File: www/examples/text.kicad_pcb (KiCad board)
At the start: 2 copper layers, 223.5 x 71.1 mm, 0 parts

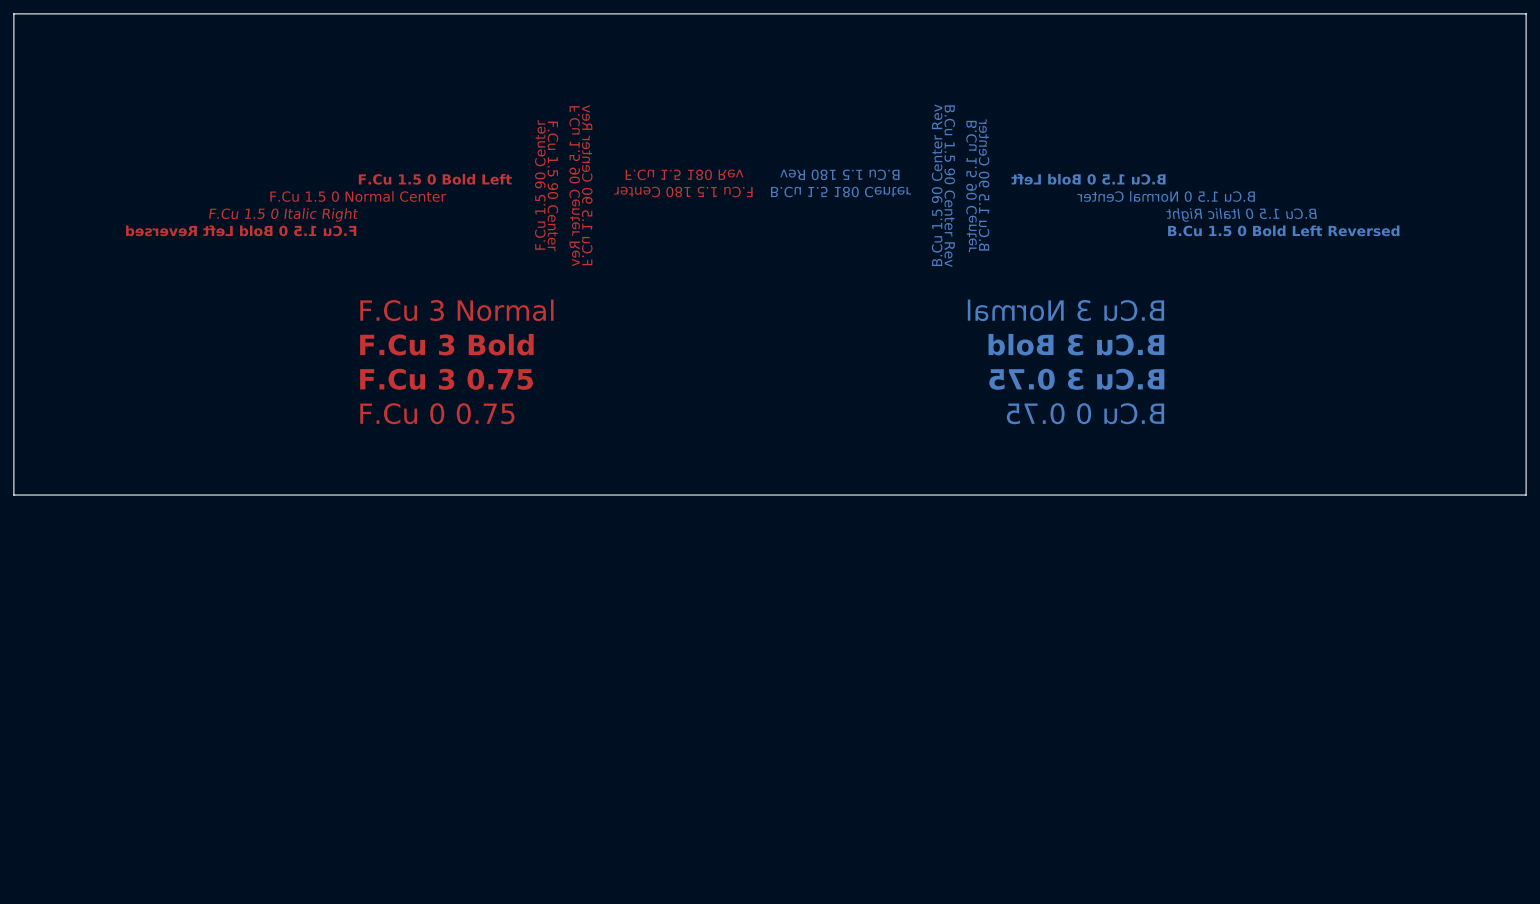
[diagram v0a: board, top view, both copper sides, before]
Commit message: Use new text engine for FpText
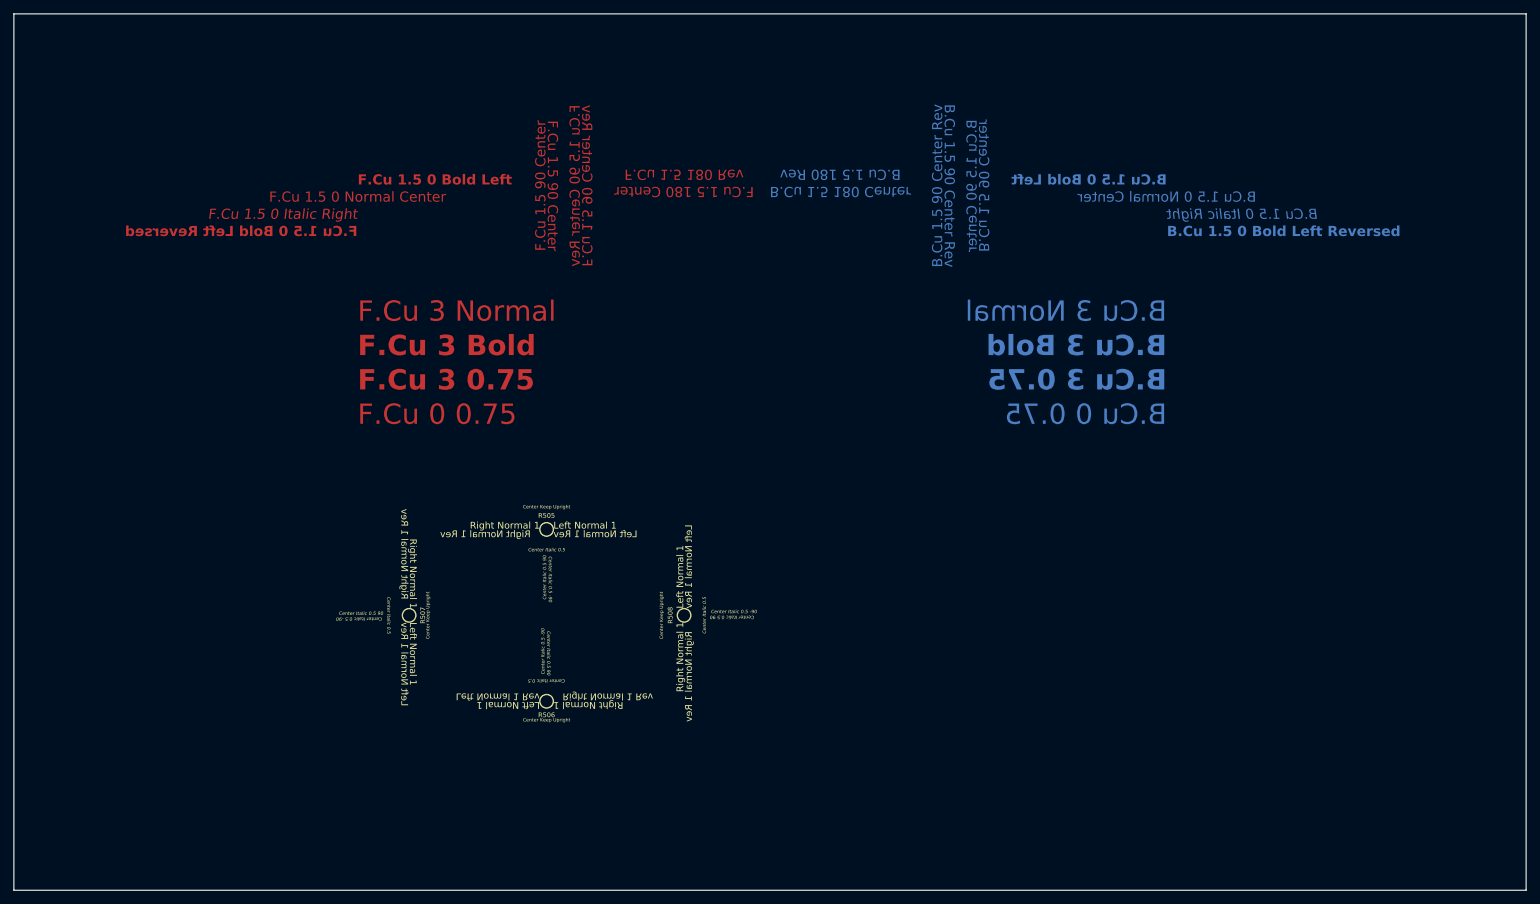
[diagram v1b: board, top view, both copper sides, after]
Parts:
- added R505: 10k, winterbloom:R_0402_HandSolder, F.Cu at (27.9, 50.8)
- added R505: 10k, winterbloom:R_0402_HandSolder, B.Cu at (94.0, 50.8)
- added R505: 10k, winterbloom:R_0402_HandSolder, B.Cu at (73.7, 63.5)
- added R505: 10k, winterbloom:R_0402_HandSolder, B.Cu at (94.0, 76.2)
- added R505: 10k, winterbloom:R_0402_HandSolder, B.Cu at (114.3, 63.5)
- added R506: 10k, winterbloom:R_0402_HandSolder, F.Cu at (27.9, 76.2)
- added R507: 10k, winterbloom:R_0402_HandSolder, F.Cu at (7.62, 63.5)
- added R508: 10k, winterbloom:R_0402_HandSolder, F.Cu at (48.3, 63.5)
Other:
- board size 223.5 x 71.1 mm -> 223.5 x 129.5 mm

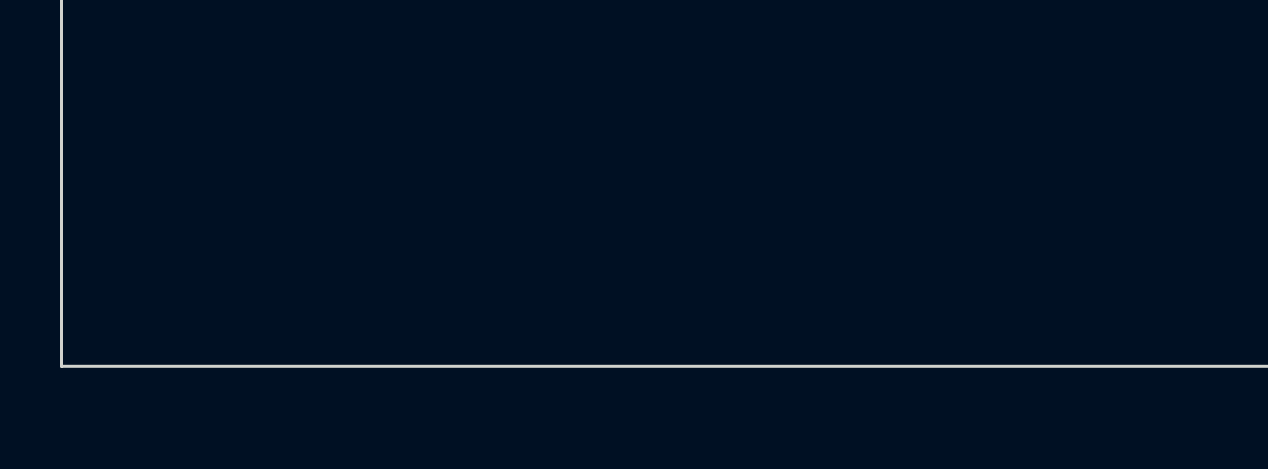
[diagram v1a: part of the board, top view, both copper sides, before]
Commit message: Add examples of custom fonts in text examples
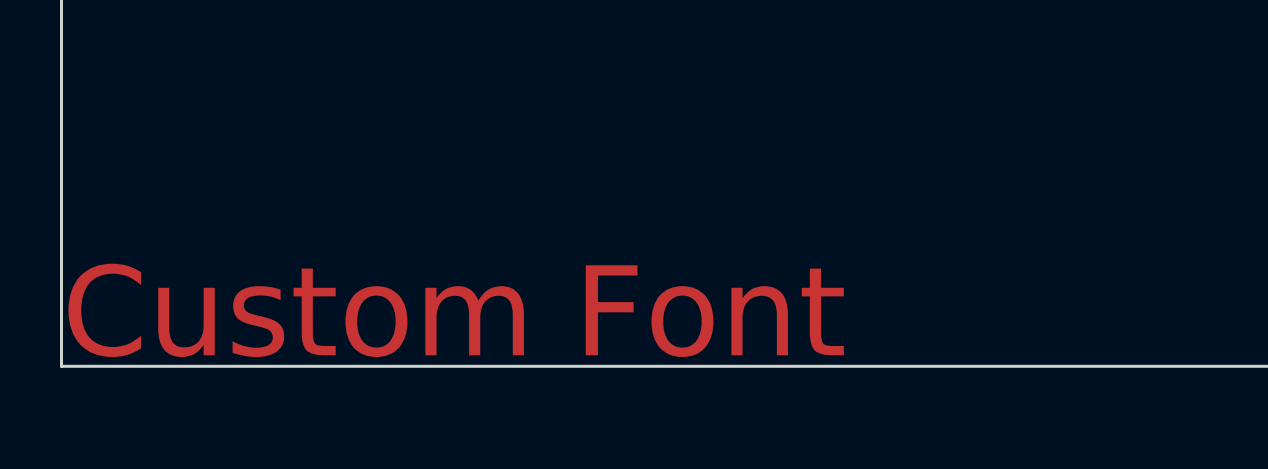
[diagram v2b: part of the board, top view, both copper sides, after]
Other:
- board text added: "Custom Font"

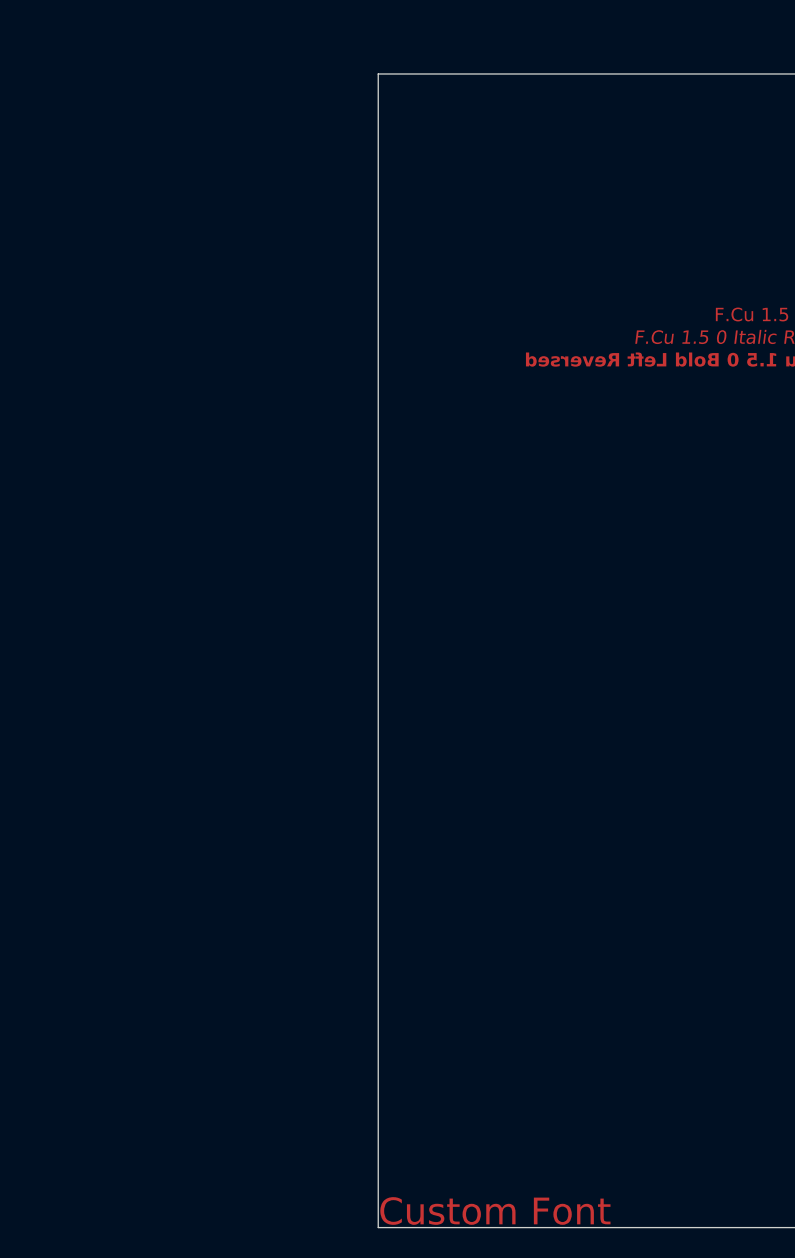
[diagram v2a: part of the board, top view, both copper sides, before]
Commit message: Fix bug in angle.rotate_point
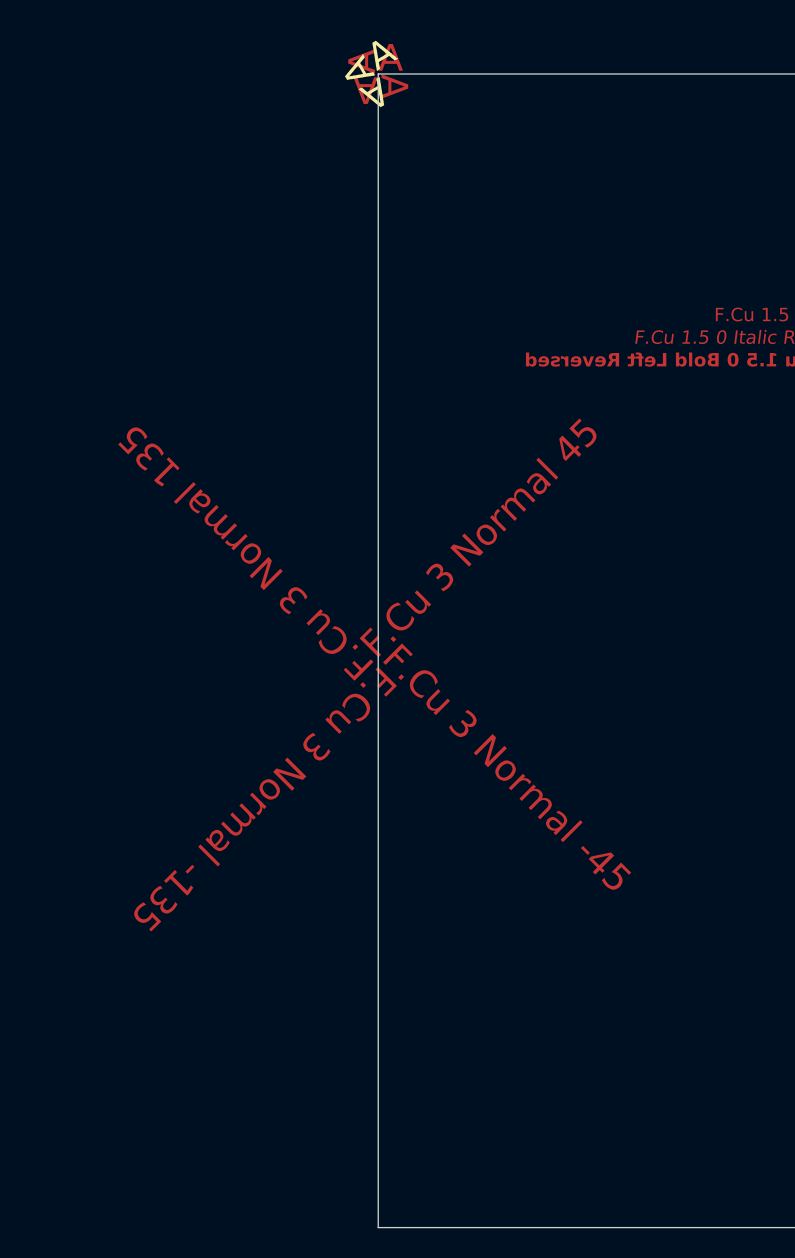
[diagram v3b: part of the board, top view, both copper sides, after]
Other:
- board text added: "A"
- board text added: "F.Cu 3 Normal -135"
- board text added: "F.Cu 3 Normal -45"
- board text added: "F.Cu 3 Normal 135"
- board text added: "F.Cu 3 Normal 45"
- board text removed: "Custom Font"

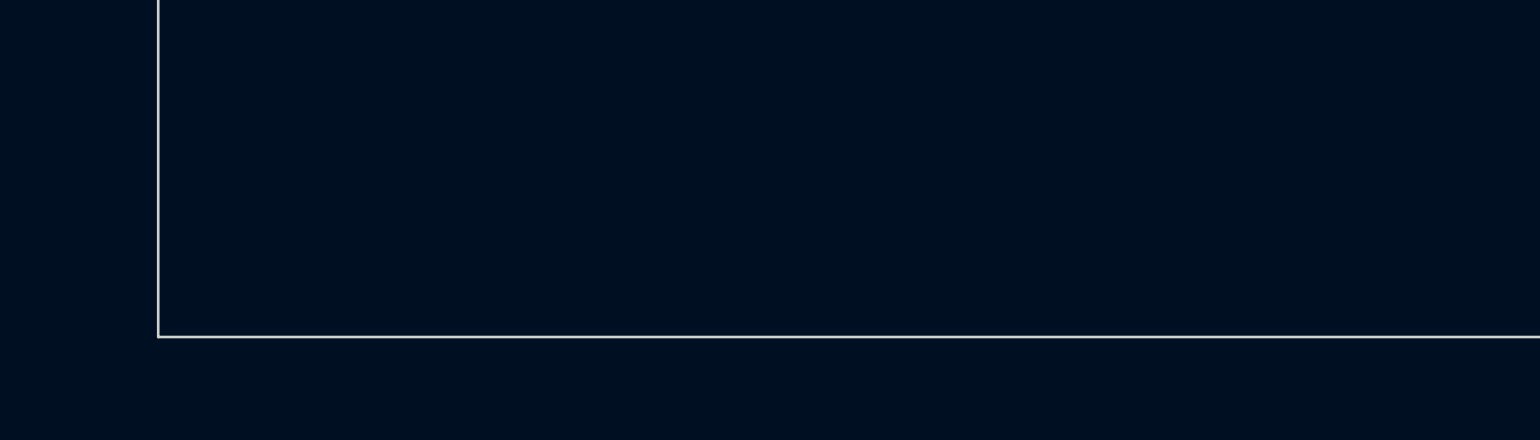
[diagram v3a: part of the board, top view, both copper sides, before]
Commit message: Add support for KiCAD 7's render_cache for board items with custom fonts.
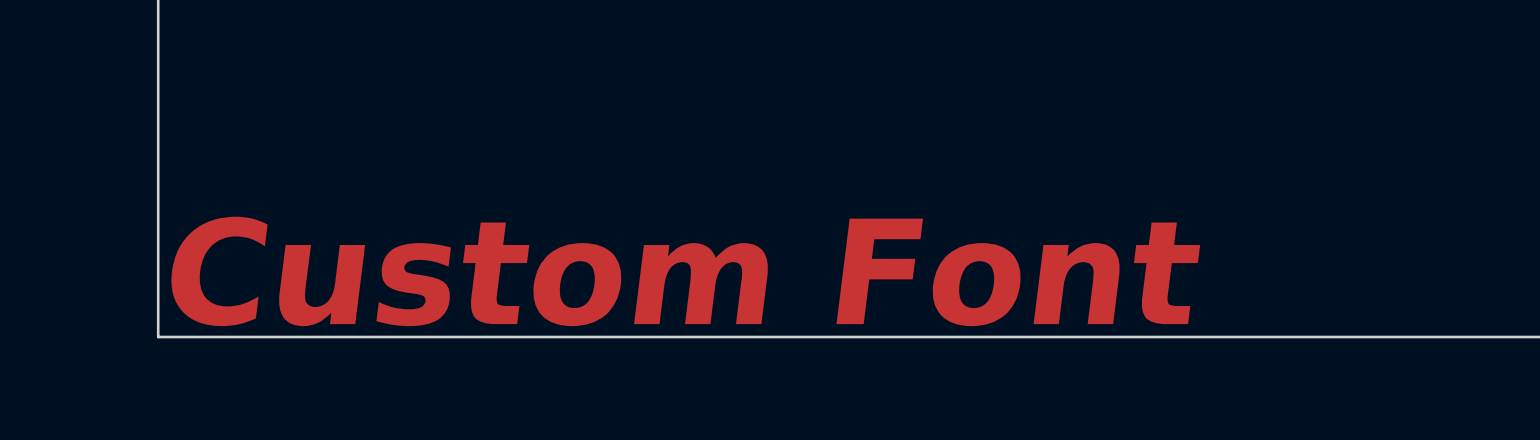
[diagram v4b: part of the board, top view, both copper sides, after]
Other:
- board text added: "Custom Font"

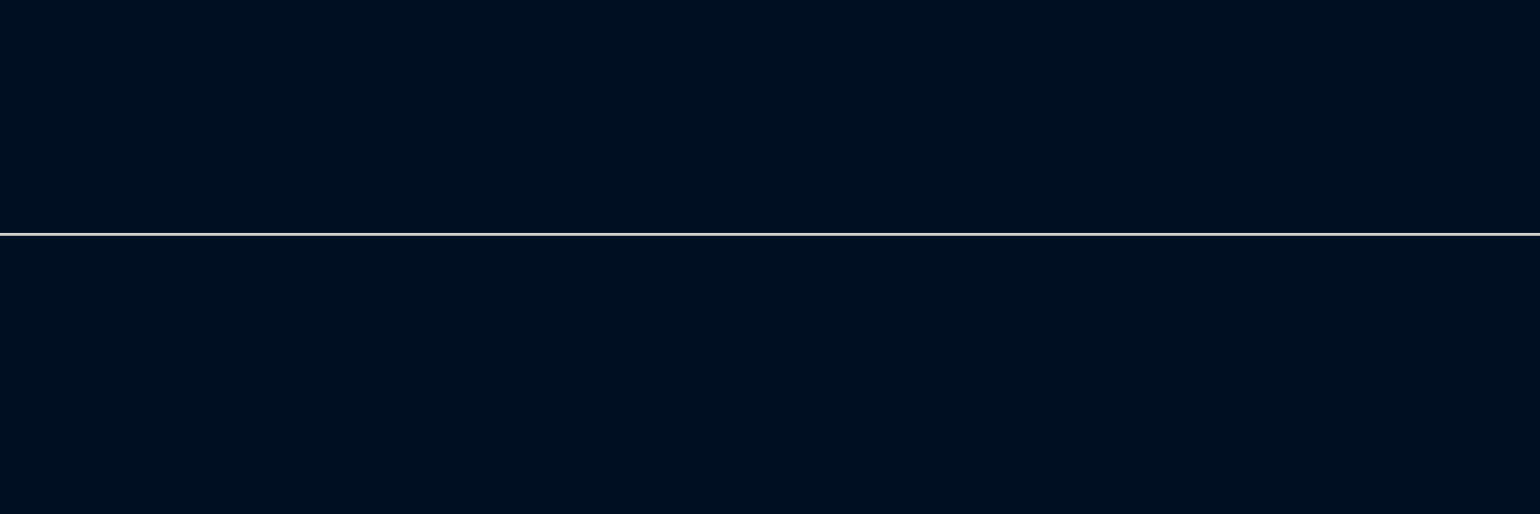
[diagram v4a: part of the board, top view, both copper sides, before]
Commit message: Fix text width/height being swapped
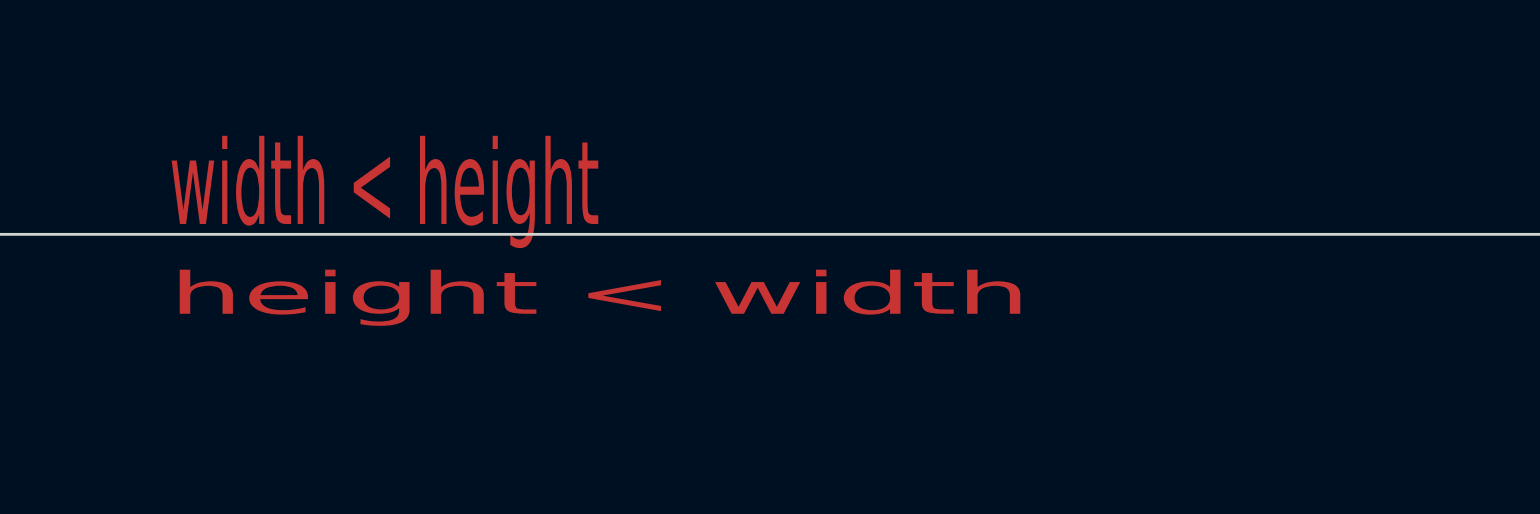
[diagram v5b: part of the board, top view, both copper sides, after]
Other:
- board text added: "height < width"
- board text added: "width < height"
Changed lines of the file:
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@@
   (setup
     (pad_to_mask_clearance 0)
+    (grid_origin -50.8 -25.4)
     (pcbplotparams
       (layerselection 0x00010fc_ffffffff)
@@
     (effects (font (size 3 3) (thickness 0.375)) (justify left bottom))
   )
+  (gr_text "width < height" (at -34.8 -25.4) (layer "F.Cu")
+    (effects (font (size 3 1.5) (thickness 0.375)) (justify left bottom))
+  )
   (gr_text "F.Cu 3 0.75" (at 0 30.48) (layer "F.Cu")
     (effects (font (size 3 3) (thickness 0.75) bold) (justify left bottom))
@@
     (effects (font (size 1.5 1.5) (thickness 0.1875) italic) (justify right bottom))
   )
+  (gr_text "height < width" (at -34.8 -22.4) (layer "F.Cu")
+    (effects (font (size 1.5 3) (thickness 0.375)) (justify left bottom))
+  )
   (gr_text "F.Cu 3 Normal 45" (at -50.8 40.64 45) (layer "F.Cu")
